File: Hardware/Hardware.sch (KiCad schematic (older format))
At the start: 65 parts, among them J1 LINEIN, J2 MICIN, J3 Raspberry_Pi_2_3, J4 LOUT, J5 HPOUT, SW1 JS5208, U1 MCP3004, U2 WM8731SEDS

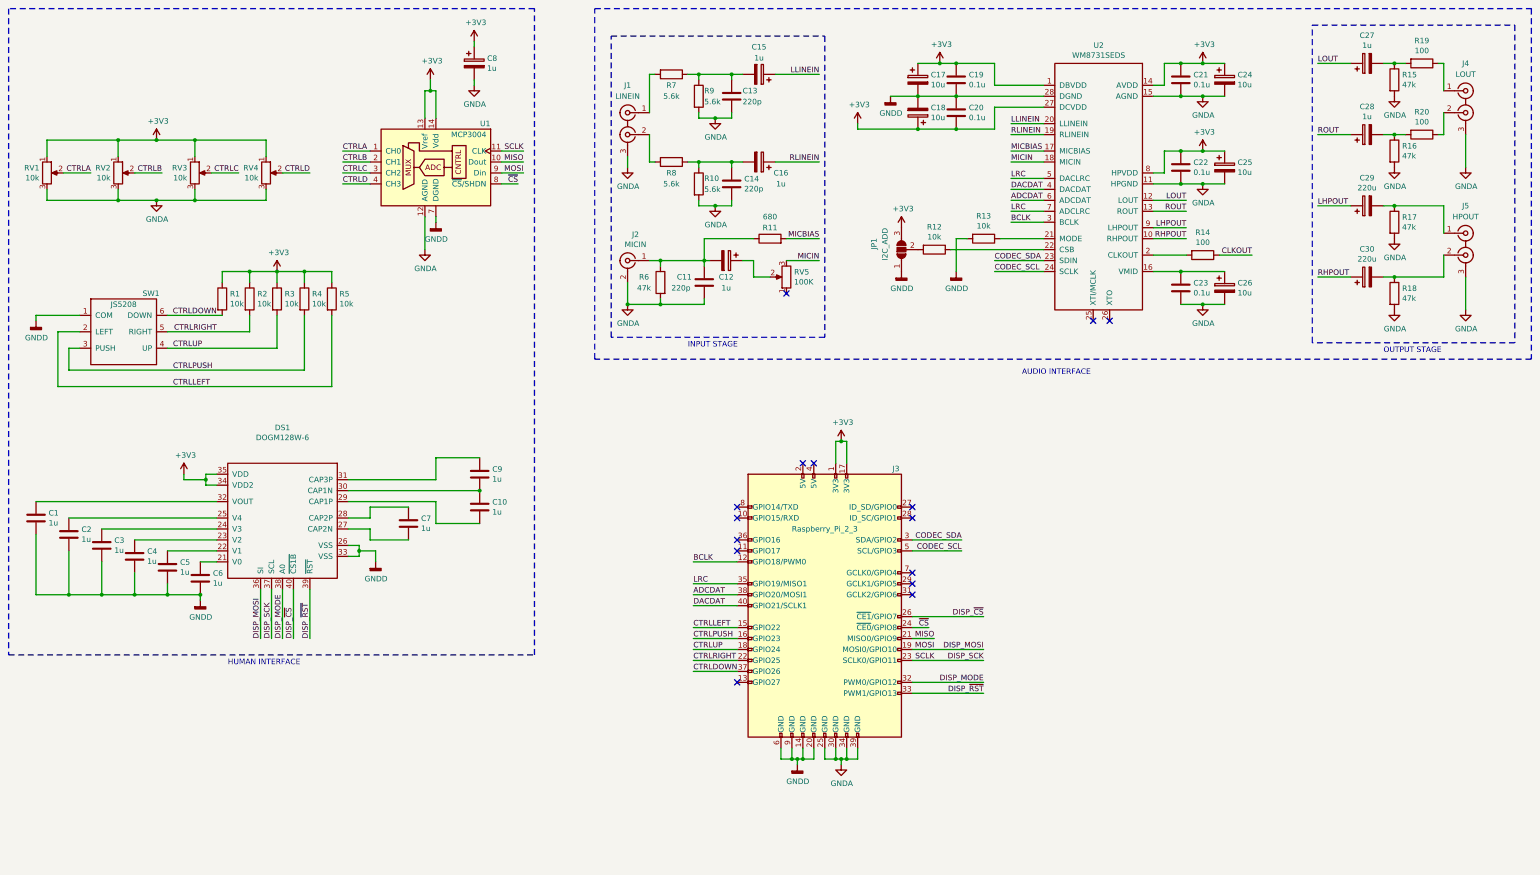
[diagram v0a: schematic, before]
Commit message: Added external oscillator to Schematic and PCB. Plotted outputs.
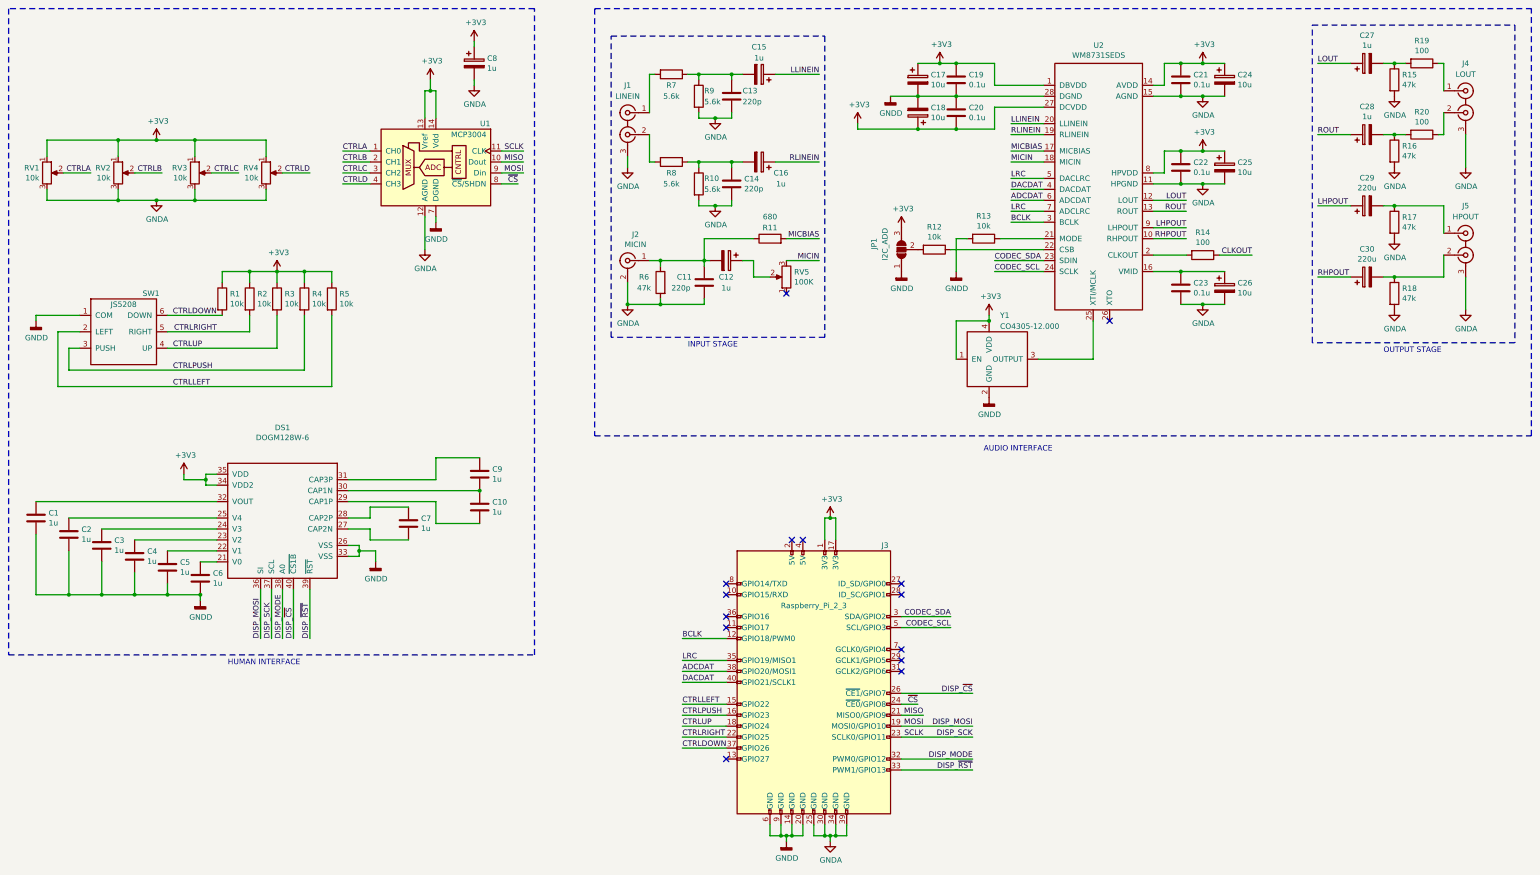
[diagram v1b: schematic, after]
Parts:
- added Y1: CO4305-12.000, signl:CO4305-12.000, symbol signl:CO4305-12.000
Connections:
- net +3V3: now also Y1.1 (EN), Y1.4 (VDD)
- net GNDD: now also Y1.2 (GND)
- net at U2.25 (XTI/MCLK): now also Y1.3 (OUTPUT)
- no-connect marks 15 -> 14
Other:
- moved on the sheet: J3

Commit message: Assigned datasheets and supplier links to all schematic components. Regenerated BoM.
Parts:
- C1, C10, C11, C13, C14, C19, C2, C20, C21, C22, C23, C3, C4, C5, C6, C7, C9: Supplier Link (none) -> https://uk.rs-online.com/web/p/mlccs-multilayer-ceramic-cap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
- C12, C15, C16, C27, C28, C8: Supplier Link (none) -> https://www.mouser.co.uk/ProductDetail/KEMET/T498B105K035AT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
- C17, C18, C24, C25, C26: Supplier Link (none) -> https://www.mouser.co.uk/ProductDetail/KEMET/T495X106K035AT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
- C29, C30: Supplier Link (none) -> https://uk.rs-online.com/web/p/aluminium-capacitors/7393488/
- DS1: Supplier Link (none) -> https://www.mouser.co.uk/ProductDetail/ELECTRONIC-ASSEMBLY/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
- J1, J4, J5: Supplier Link (none) -> https://www.rapidonline.com/jyk-p2500-03-3-pole-straight-he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
- J2: Supplier Link (none) -> https://www.rapidonline.com/jyk-p2500-02-2-pole-straight-he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
- J3: Supplier Link (none) -> https://uk.rs-online.com/web/p/processor-microcontroller-de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
- R1, R10, R11, R12, R13, R14, R15, R16, R17, R18, R19, R2, R20, R3, R4, R5, R6, R7, R8, R9: Supplier Link (none) -> https://uk.rs-online.com/web/p/surface-mount-fixed-resistor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
- RV1, RV2, RV3, RV4: Supplier Link (none) -> https://www.rapidonline.com/taiwan-alpha-rv16af-20-20k-b10k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
- RV5: Supplier Link (none) -> https://www.rapidonline.com/taiwan-alpha-rv16af-100k-lin-16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
- SW1: Supplier Link (none) -> https://www.mouser.co.uk/ProductDetail/E-Switch/JS5208?qs=f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
- U1: Supplier Link (none) -> https://www.mouser.co.uk/ProductDetail/Microchip-Technology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
- U2: Supplier Link (none) -> https://www.mouser.co.uk/ProductDetail/Cirrus-Logic/WM8731S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
- Y1: Supplier Link (none) -> https://uk.rs-online.com/web/p/crystal-oscillators/7079659/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
